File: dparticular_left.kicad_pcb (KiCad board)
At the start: 2 copper layers, 51 parts, among them J1 To Left Hand, SW1:10 Key_Ins, SW1:11 Key_Prnt, SW2:10 Key_F7, SW2:11 Key_F8, SW2:12 Key_F9, SW2:13 Key_F10, SW2:14 Key_F11, SW2:15 Key_F12, SW2:16 Key_Del, SW3:10 Key_7, SW3:11 Key_8, SW3:12 Key_9, SW3:13 Key_0, SW3:14 Key_Hyph, SW3:15 Key_Eql, SW3:16 Key_Bksp, SW3:9 Key_6, SW4:10 Key_U, SW4:11 Key_I, SW4:12 Key_O, SW4:13 Key_P, SW4:14 Key_LBrk, SW4:15 Key_RBrk, SW4:16 Key_BkSl, SW4:9 Key_Y, SW5:10 Key_J, SW5:11 Key_K, SW5:12 Key_L, SW5:13 Key_Semi, SW5:14 Key_Quot, SW5:16 Key_Entr, SW5:9 Key_H, SW6:10 Key_M, SW6:11 Key_Coma, SW6:12 Key_Per, SW6:13 Key_Slsh, SW6:14 Key_RShft, SW6:9 Key_N, SW7:11 Key_RAlt, SW7:12 Key_RWin, SW7:13 Key_Menu, SW7:14 Key_RCtrl, SW7:9 Key_RSpc, U1 MCP23018

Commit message: Preliminary placements for left hand
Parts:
- removed C1, C2, C3: 0.1uF, Capacitor_THT:C_Disc_D5.1mm_W3.2mm_P5.00mm
- removed D1, D2, D3: APA-106-F5, LED_THT:LED_D5.0mm-4_RGB
- removed J1: To Left Hand, Connector_PinHeader_1.00mm:PinHeader_1x06_P1.00mm_Horizontal
- removed SW1:10: Key_Ins, dparticular:MX_W_DIODE
- removed SW1:11: Key_Prnt, dparticular:MX_W_DIODE
- removed SW2:10: Key_F7, dparticular:MX_W_DIODE
- removed SW2:11: Key_F8, dparticular:MX_W_DIODE
- removed SW2:12: Key_F9, dparticular:MX_W_DIODE
- removed SW2:13: Key_F10, dparticular:MX_W_DIODE
- removed SW2:14: Key_F11, dparticular:MX_W_DIODE
- removed SW2:15: Key_F12, dparticular:MX_W_DIODE
- removed SW2:16: Key_Del, dparticular:MX_W_DIODE
- removed SW3:10: Key_7, dparticular:MX_W_DIODE
- removed SW3:11: Key_8, dparticular:MX_W_DIODE
- removed SW3:12: Key_9, dparticular:MX_W_DIODE
- removed SW3:13: Key_0, dparticular:MX_W_DIODE
- removed SW3:14: Key_Hyph, dparticular:MX_W_DIODE
- removed SW3:15: Key_Eql, dparticular:MX_W_DIODE
- removed SW3:16: Key_Bksp, dparticular:MX_W_DIODE
- removed SW3:9: Key_6, dparticular:MX_W_DIODE
- removed SW4:10: Key_U, dparticular:MX_W_DIODE
- removed SW4:11: Key_I, dparticular:MX_W_DIODE
- removed SW4:12: Key_O, dparticular:MX_W_DIODE
- removed SW4:13: Key_P, dparticular:MX_W_DIODE
- removed SW4:14: Key_LBrk, dparticular:MX_W_DIODE
- removed SW4:15: Key_RBrk, dparticular:MX_W_DIODE
- removed SW4:16: Key_BkSl, dparticular:MX_W_DIODE
- removed SW4:9: Key_Y, dparticular:MX_W_DIODE
- removed SW5:10: Key_J, dparticular:MX_W_DIODE
- removed SW5:11: Key_K, dparticular:MX_W_DIODE
- removed SW5:12: Key_L, dparticular:MX_W_DIODE
- removed SW5:13: Key_Semi, dparticular:MX_W_DIODE
- removed SW5:14: Key_Quot, dparticular:MX_W_DIODE
- removed SW5:16: Key_Entr, dparticular:MX_W_DIODE
- removed SW5:9: Key_H, dparticular:MX_W_DIODE
- removed SW6:10: Key_M, dparticular:MX_W_DIODE
- removed SW6:11: Key_Coma, dparticular:MX_W_DIODE
- removed SW6:12: Key_Per, dparticular:MX_W_DIODE
- removed SW6:13: Key_Slsh, dparticular:MX_W_DIODE
- removed SW6:14: Key_RShft, dparticular:MX_W_DIODE
- removed SW6:9: Key_N, dparticular:MX_W_DIODE
- removed SW7:11: Key_RAlt, dparticular:MX_W_DIODE
- removed SW7:12: Key_RWin, dparticular:MX_W_DIODE
- removed SW7:13: Key_Menu, dparticular:MX_W_DIODE
- removed SW7:14: Key_RCtrl, dparticular:MX_W_DIODE
- removed SW7:9: Key_RSpc, dparticular:MX_W_DIODE
- removed U1: MCP23018, Package_DIP:DIP-28_W7.62mm_LongPads
- added J2: USB from outside, Connector_PinHeader_1.00mm:PinHeader_1x04_P1.00mm_Horizontal, F.Cu at (164.3, 28.6)
- added J3: To Right Hand, Connector_PinHeader_1.00mm:PinHeader_1x06_P1.00mm_Horizontal, F.Cu at (50.0, 68.8)
- added J4: Jumper to Teensy USB, Connector_PinHeader_1.00mm:PinHeader_1x04_P1.00mm_Vertical, F.Cu at (150.0, 36.3)
- added R1: 4.7k, Resistor_THT:R_Axial_DIN0207_L6.3mm_D2.5mm_P7.62mm_Horizontal, F.Cu at (64.3, 73.8)
- added R2: 4.7k, Resistor_THT:R_Axial_DIN0207_L6.3mm_D2.5mm_P7.62mm_Horizontal, F.Cu at (64.3, 69.1)
- added SW1:6: Key_Scrl, dparticular:MX_W_DIODE, F.Cu at (76.2, 33.3)
- added SW1:7: Key_Paus, dparticular:MX_W_DIODE, F.Cu at (57.1, 33.3)
- added SW2:1: Key_ESC, dparticular:MX_W_DIODE, F.Cu at (195.3, 57.1)
- added SW2:2: Key_F1, dparticular:MX_W_DIODE, F.Cu at (157.2, 57.1)
- added SW2:3: Key_F2, dparticular:MX_W_DIODE, F.Cu at (138.1, 57.1)
- added SW2:4: Key_F3, dparticular:MX_W_DIODE, F.Cu at (119.1, 57.1)
- added SW2:5: Key_F4, dparticular:MX_W_DIODE, F.Cu at (100.0, 57.1)
- added SW2:6: Key_F5, dparticular:MX_W_DIODE, F.Cu at (76.2, 57.1)
- added SW2:7: Key_F6, dparticular:MX_W_DIODE, F.Cu at (57.1, 57.1)
- added SW3:1: Key_Home, dparticular:MX_W_DIODE, F.Cu at (195.3, 90.5)
- added SW3:2: Key_End, dparticular:MX_W_DIODE, F.Cu at (176.2, 90.5)
- added SW3:3: Key_Tilde, dparticular:MX_W_DIODE, F.Cu at (138.1, 90.5)
- added SW3:4: Key_1, dparticular:MX_W_DIODE, F.Cu at (119.1, 90.5)
- added SW3:5: Key_2, dparticular:MX_W_DIODE, F.Cu at (100.0, 88.1)
- added SW3:6: Key_3, dparticular:MX_W_DIODE, F.Cu at (81.0, 85.7)
- added SW3:7: Key_4, dparticular:MX_W_DIODE, F.Cu at (61.9, 88.1)
- added SW3:8: Key_5, dparticular:MX_W_DIODE, F.Cu at (42.9, 90.5)
- added SW4:2: Key_PgUp, dparticular:MX_W_DIODE, F.Cu at (185.7, 109.5)
- added SW4:3: Key_Tab, dparticular:MX_W_DIODE, F.Cu at (142.9, 109.5)
- added SW4:4: Key_Q, dparticular:MX_W_DIODE, F.Cu at (119.1, 109.5)
- added SW4:5: Key_W, dparticular:MX_W_DIODE, F.Cu at (100.0, 107.2)
- added SW4:6: Key_E, dparticular:MX_W_DIODE, F.Cu at (81.0, 104.8)
- added SW4:7: Key_R, dparticular:MX_W_DIODE, F.Cu at (61.9, 107.2)
- added SW4:8: Key_T, dparticular:MX_W_DIODE, F.Cu at (42.9, 109.5)
- added SW5:2: Key_PgDn, dparticular:MX_W_DIODE, F.Cu at (185.7, 128.6)
- added SW5:3: Key_Caps, dparticular:MX_W_DIODE, F.Cu at (145.3, 128.6)
- added SW5:4: Key_A, dparticular:MX_W_DIODE, F.Cu at (119.1, 128.6)
- added SW5:5: Key_S, dparticular:MX_W_DIODE, F.Cu at (100.0, 126.2)
- added SW5:6: Key_D, dparticular:MX_W_DIODE, F.Cu at (81.0, 123.8)
- added SW5:7: Key_F, dparticular:MX_W_DIODE, F.Cu at (61.9, 126.2)
- added SW5:8: Key_G, dparticular:MX_W_DIODE, F.Cu at (42.9, 128.6)
- added SW6:3: Key_LShft, dparticular:MX_W_DIODE, F.Cu at (150.0, 147.6)
- added SW6:4: Key_Z, dparticular:MX_W_DIODE, F.Cu at (119.1, 147.6)
- added SW6:5: Key_X, dparticular:MX_W_DIODE, F.Cu at (100.0, 145.3)
- added SW6:6: Key_C, dparticular:MX_W_DIODE, F.Cu at (81.0, 142.9)
- added SW6:7: Key_V, dparticular:MX_W_DIODE, F.Cu at (61.9, 145.3)
- added SW6:8: Key_B, dparticular:MX_W_DIODE, F.Cu at (42.9, 147.6)
- added SW7:3: Key_LCtrl, dparticular:MX_W_DIODE, F.Cu at (157.2, 166.7)
- added SW7:4: Key_Fn, dparticular:MX_W_DIODE, F.Cu at (126.2, 171.4)
- added SW7:5: Key_LWin, dparticular:MX_W_DIODE, F.Cu at (102.4, 171.4)
- added SW7:6: Key_LAlt, dparticular:MX_W_DIODE, F.Cu at (76.2, 171.4)
- added SW7:8: Key_LSpc, dparticular:MX_W_DIODE, F.Cu at (40.5, 171.4)
- added U2: TEENSY2.0_ONLY_EDGES, dparticular:TEENSY_2.0_EDGES_ONLY, F.Cu at (105.1, 33.8)

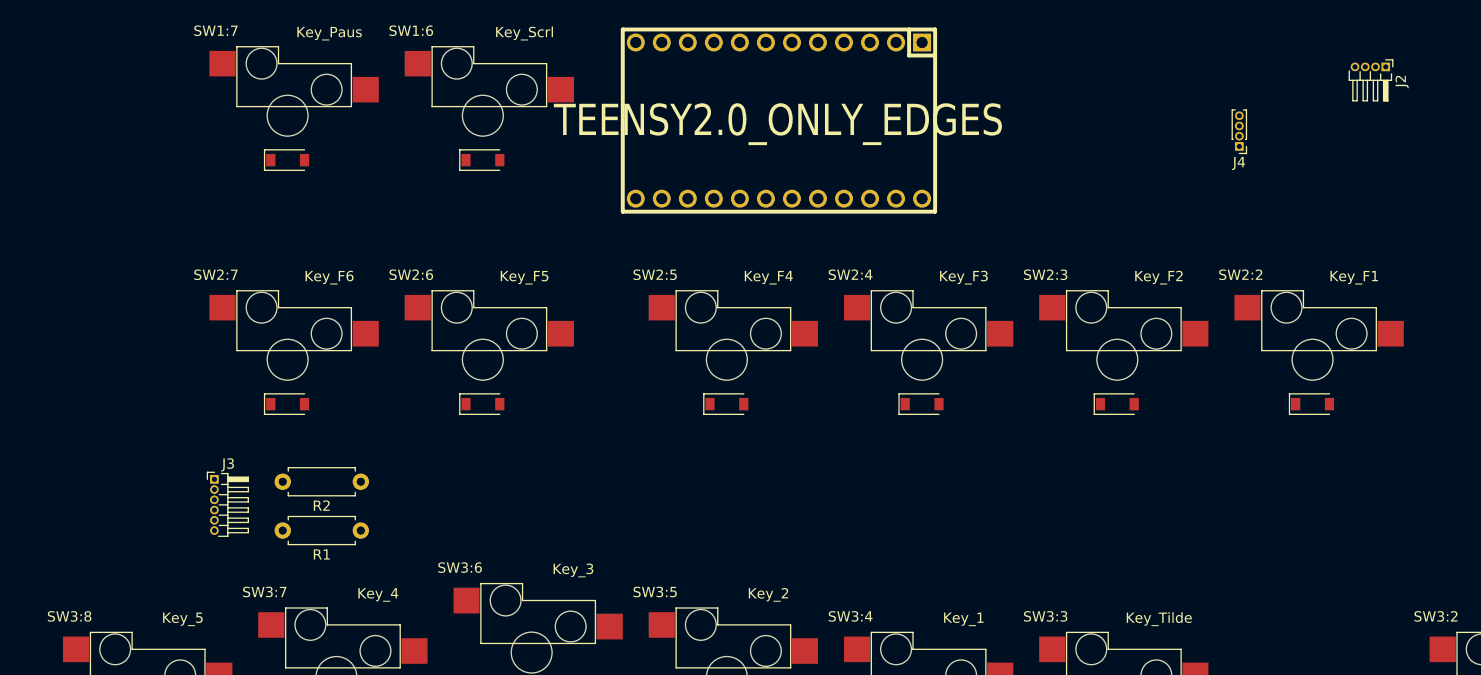
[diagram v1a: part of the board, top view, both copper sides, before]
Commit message: Fixed footprints on switches and headers
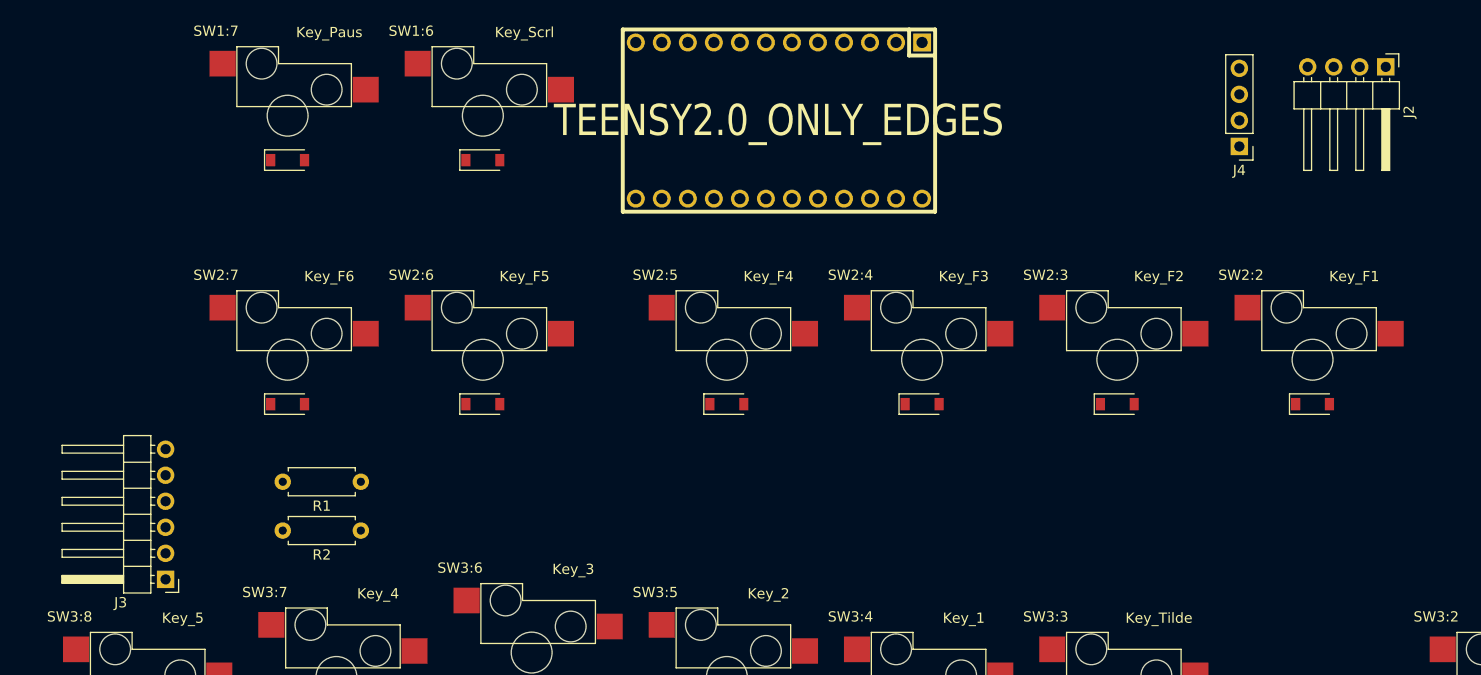
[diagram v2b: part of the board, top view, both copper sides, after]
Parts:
- J2: footprint Connector_PinHeader_1.00mm:PinHeader_1x04_P1.00mm_Horizontal -> Connector_PinHeader_2.54mm:PinHeader_1x04_P2.54mm_Horizontal
- J3: footprint Connector_PinHeader_1.00mm:PinHeader_1x06_P1.00mm_Horizontal -> Connector_PinHeader_2.54mm:PinHeader_1x06_P2.54mm_Horizontal
- J4: footprint Connector_PinHeader_1.00mm:PinHeader_1x04_P1.00mm_Vertical -> Connector_PinHeader_2.54mm:PinHeader_1x04_P2.54mm_Vertical
- moved J3 10.9 mm to (45.2, 78.6), turned to 180 degrees
- moved R1 4.76 mm to (64.3, 69.1)
- moved R2 4.76 mm to (64.3, 73.8)
